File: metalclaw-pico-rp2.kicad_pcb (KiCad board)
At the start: 4 copper layers, 21 x 51 mm, 123 parts, among them J1 USB4105-GF-A, J2 FTSH-105-01-L-DV-K, SW1 PTS810SJM250SMTR LFS, SW2 PTS810SJM250SMTR LFS, U1 XC6220B331MR-G, U2 RP2354B, U3 APS6404L-3SQR-SN, Y1 ABM8-272-T3

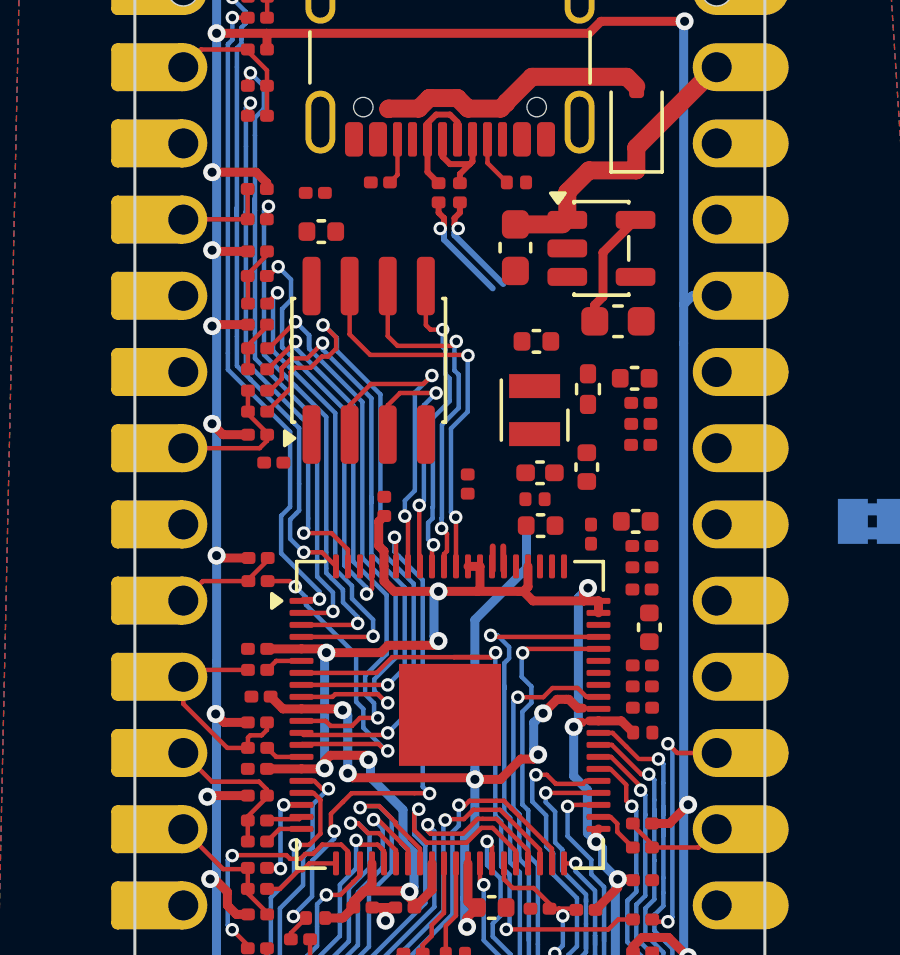
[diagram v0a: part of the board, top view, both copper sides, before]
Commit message: Route USB and last quadrant signals
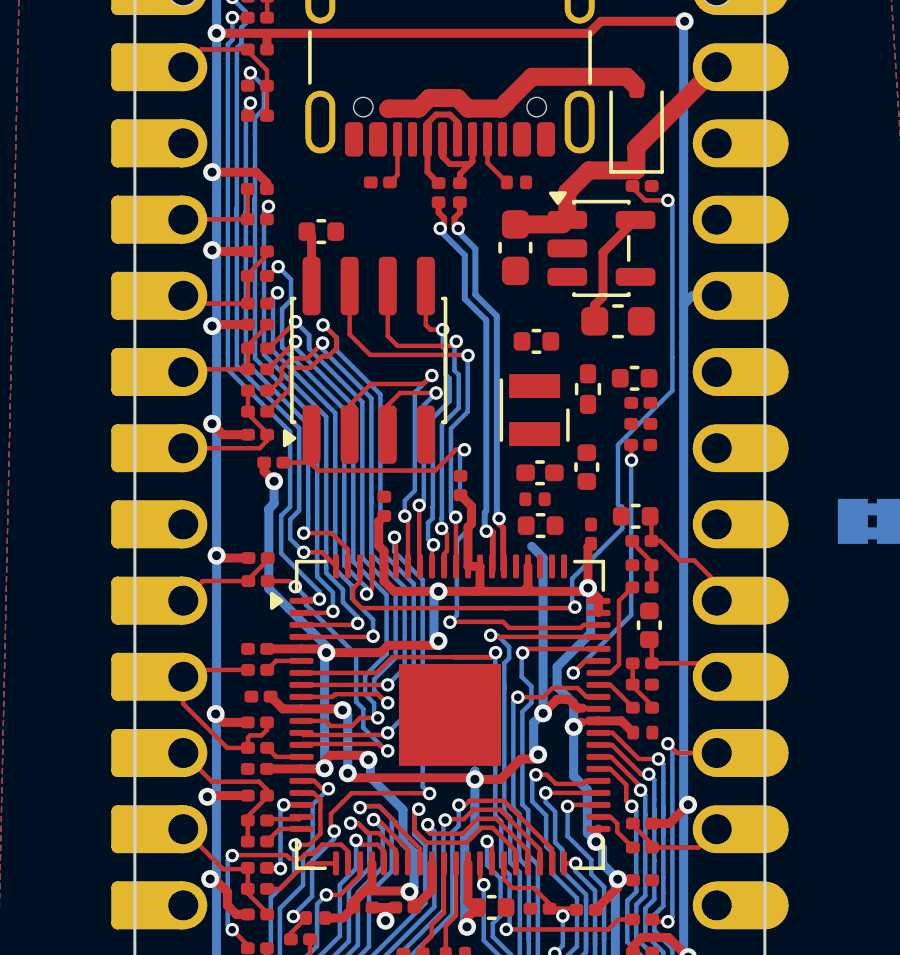
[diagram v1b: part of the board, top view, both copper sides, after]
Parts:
- moved R34 10.9 mm to (170.2, 81.2)
- moved C14 0.25 mm to (164.2, 91.2)
- moved C5 0.17 mm to (170.0, 92.2)
- moved R24 0.17 mm to (170.2, 93.1)
- moved C6 0.07 mm to (170.5, 95.9)
- moved C8 0.07 mm to (170.2, 93.9)
- moved R26 0.07 mm to (170.2, 97.2)
- moved R31 0.07 mm to (170.2, 94.6)
- moved C7 0.06 mm to (170.2, 97.9)
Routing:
- net Net-(U2-GPIO1): track 0.00 -> 25.5 mm, vias 0 -> 2
- net Net-(U2-GPIO47/ADC7): track 0.00 -> 18.8 mm, vias 0 -> 2
- net +3V3: track 72.3 -> 86.0 mm, vias 11 -> 12
- net /GP28: track 0.00 -> 9.42 mm, vias 0 -> 2
- net /USB_D+: track 4.55 -> 13.3 mm, vias 1 -> 2
- net /USB_D-: track 4.37 -> 13.0 mm, vias 1 -> 2
- net Net-(A1-GPIO27_ADC1): track 0.00 -> 4.18 mm
- net /GP27: track 0.00 -> 3.55 mm
- net Net-(A1-GPIO26_ADC0): track 0.00 -> 3.17 mm
- net Net-(U2-VREG_FB): track 31.9 -> 28.8 mm
- net /GP3: track 2.01 -> 4.27 mm
- net /GP4: track 1.75 -> 3.95 mm
- net Net-(C8-Pad2): track 0.00 -> 1.82 mm
- net Net-(C7-Pad2): track 0.00 -> 1.75 mm
- net /GP26: track 0.00 -> 1.47 mm

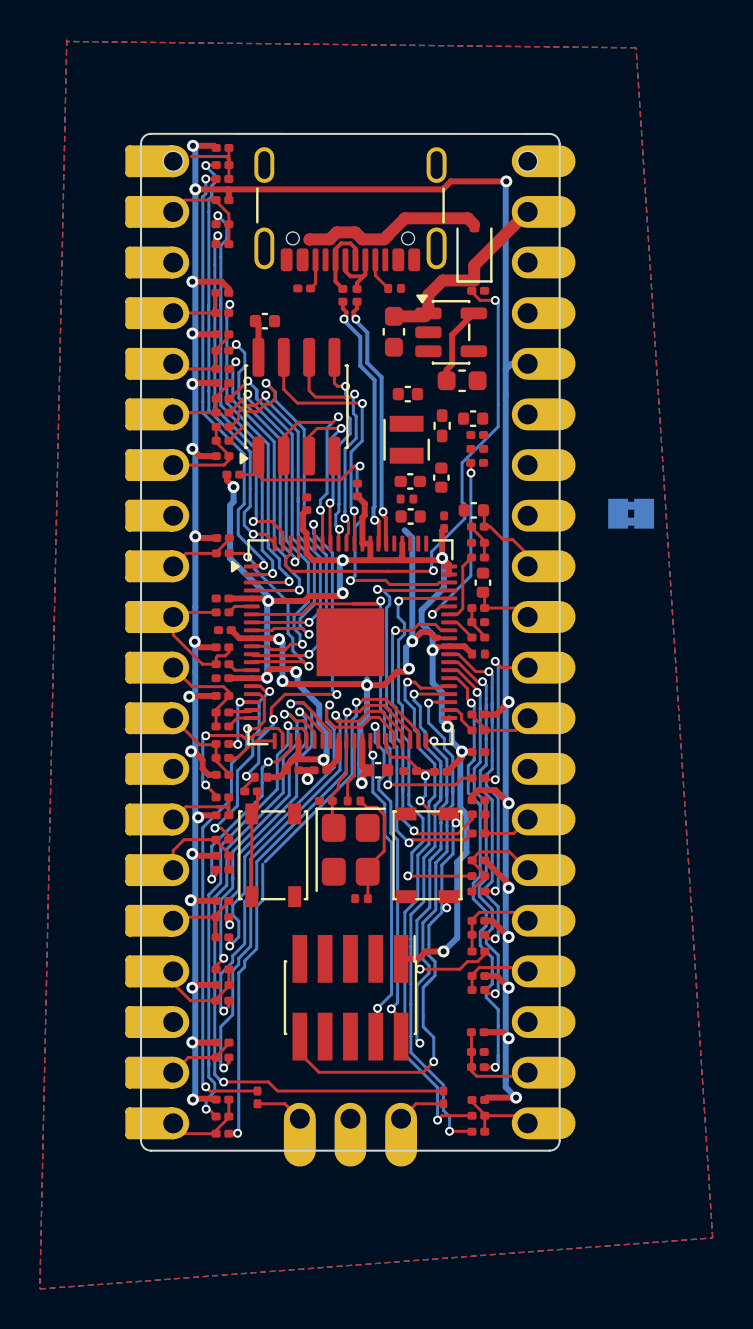
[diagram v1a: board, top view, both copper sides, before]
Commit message: Route all signals
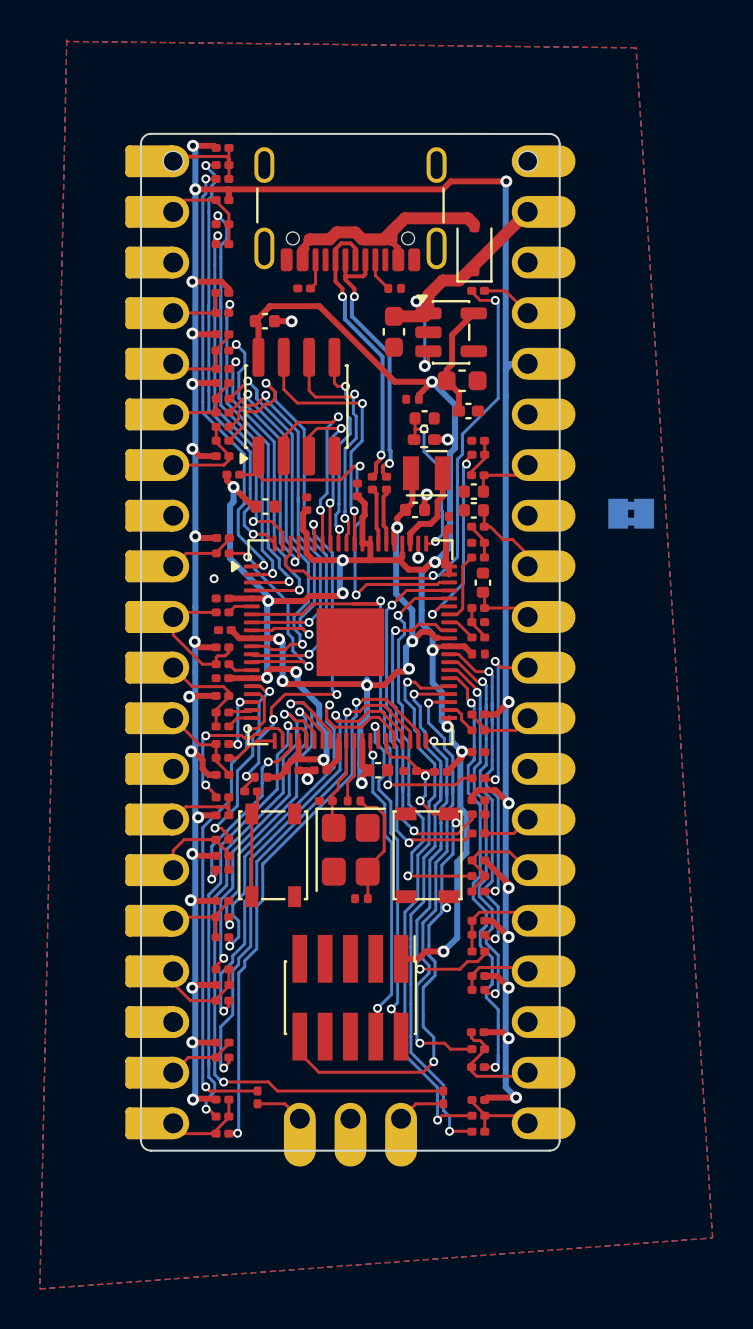
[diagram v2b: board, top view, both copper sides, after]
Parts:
- moved R80 9.54 mm to (165.6, 90.9)
- moved R81 9.54 mm to (164.9, 90.9)
- moved C12 9.10 mm to (159.6, 92.1)
- moved C15 5.01 mm to (166.9, 86.7), turned to 0 degrees
- moved C11 4.58 mm to (169.7, 87.3)
- moved C4 3.66 mm to (170.0, 91.3)
- moved C10 3.09 mm to (167.5, 87.6), turned to 180 degrees
- moved R23 2.02 mm to (170.2, 90.5)
- moved L1 1.96 mm to (167.6, 90.4), turned to 0 degrees
- moved R73 1.13 mm to (167.5, 88.7), turned to 180 degrees
- moved R32 0.41 mm to (170.2, 89.5)
- moved C9 0.41 mm to (170.2, 88.8)
- moved C13 0.40 mm to (167.1, 92.2)
- moved C22 0.23 mm to (168.7, 92.9)
- moved R67 0.14 mm to (170.2, 119.3), turned to 180 degrees
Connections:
- J1 pad A6: Net-(J1-D+-PadA6) -> /USB_D+
- J1 pad A7: Net-(J1-D--PadA7) -> /USB_D-
- J1 pad B6: Net-(J1-D+-PadA6) -> /USB_D+
- J1 pad B7: Net-(J1-D--PadA7) -> /USB_D-
- R80 pad 1: Net-(J1-D--PadA7) -> /USB_D-
- R80 pad 2: /USB_D- -> Net-(U2-USB_DM)
- R81 pad 1: Net-(J1-D+-PadA6) -> /USB_D+
- R81 pad 2: /USB_D+ -> Net-(U2-USB_DP)
- U2 pad 66: /USB_D- -> Net-(U2-USB_DM)
- U2 pad 67: /USB_D+ -> Net-(U2-USB_DP)
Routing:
- net +3V3: track 86.0 -> 112.5 mm, vias 12 -> 14
- net Net-(U2-VREG_AVDD): track 0.00 -> 8.21 mm, vias 0 -> 2
- net Net-(D1-A): track 9.15 -> 15.0 mm
- net Net-(U2-VREG_LX): track 0.00 -> 4.91 mm
- net VS: track 9.66 -> 14.3 mm, vias 0 -> 2
- net Net-(U2-VREG_FB): track 28.8 -> 33.1 mm, vias 6 -> 7
- net Net-(J1-D+-PadA6): track 3.95 -> 0.00 mm
- net Net-(A1-GPIO28_ADC2): track 0.00 -> 3.23 mm
- net Net-(J1-D--PadA7): track 3.22 -> 0.00 mm
- net Net-(U2-USB_DM): track 0.00 -> 2.85 mm
- net Net-(U2-USB_DP): track 0.00 -> 2.84 mm
- net /3V3_EN: track 0.00 -> 2.63 mm
- net Net-(U2-GPIO34): track 20.3 -> 22.8 mm
- net GND: track 1.53 -> 3.93 mm, vias 1 -> 5
- net Net-(C9-Pad2): track 0.00 -> 2.01 mm
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
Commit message: Rearrange power passives
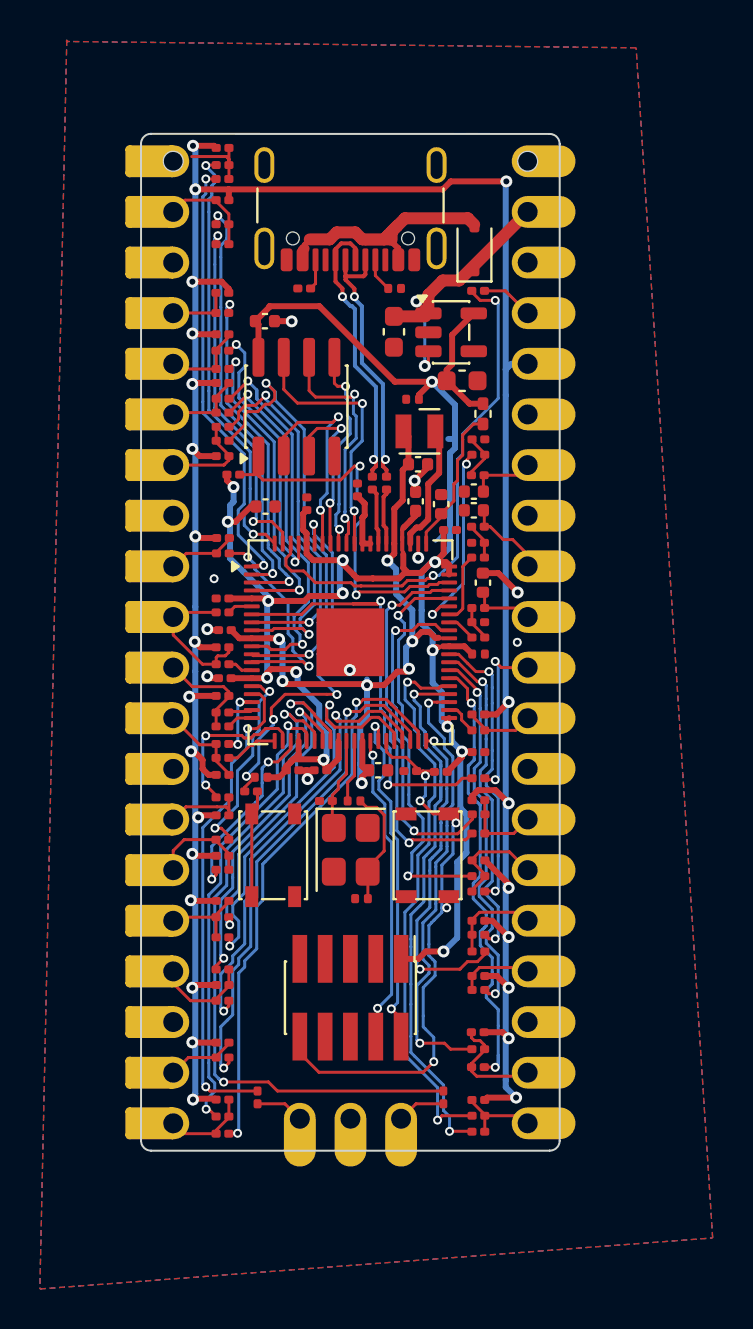
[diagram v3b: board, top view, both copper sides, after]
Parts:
- removed JP1: Jumper_2_Bridged, Jumper:SolderJumper-2_P1.3mm_Bridged2Bar_Pad1.0x1.5mm
- moved C11 5.25 mm to (167.1, 91.8), turned to -90 degrees
- moved C10 4.38 mm to (168.4, 91.9), turned to -90 degrees
- moved R73 3.22 mm to (170.5, 87.4), turned to -90 degrees
- moved C13 2.29 mm to (167.2, 89.9)
- moved L1 2.13 mm to (167.3, 88.3)
- moved C22 0.37 mm to (168.8, 93.2), turned to 180 degrees
- moved C18 0.12 mm to (157.5, 100.7)
- moved C9 0.07 mm to (170.2, 88.7), turned to 180 degrees
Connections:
- A1 pad 33: Net-(A1-AGND) -> GND
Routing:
- net GND: track 3.93 -> 8.82 mm, vias 5 -> 10
- net +3V3: track 112.5 -> 117.2 mm
- net Net-(U2-VREG_LX): track 4.91 -> 6.81 mm
- net Net-(U2-VREG_FB): track 33.1 -> 34.3 mm
- net Net-(U2-GPIO40/ADC0): track 15.1 -> 14.5 mm
- net Net-(U2-GPIO25): track 35.1 -> 34.5 mm
- net /BOOTSEL: track 19.0 -> 19.6 mm
- net Net-(U2-VREG_AVDD): track 8.21 -> 7.96 mm, vias 2 -> 0

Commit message: Fix overlap DRC errors
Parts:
- moved L1 0.09 mm to (167.3, 88.2)
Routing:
- net Net-(U2-GPIO46/ADC6): track 19.0 -> 20.2 mm
- net Net-(U2-GPIO41/ADC1): track 17.0 -> 17.5 mm
- net Net-(U2-VREG_AVDD): track 7.96 -> 7.46 mm
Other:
- board text removed: "${REFERENCE}"

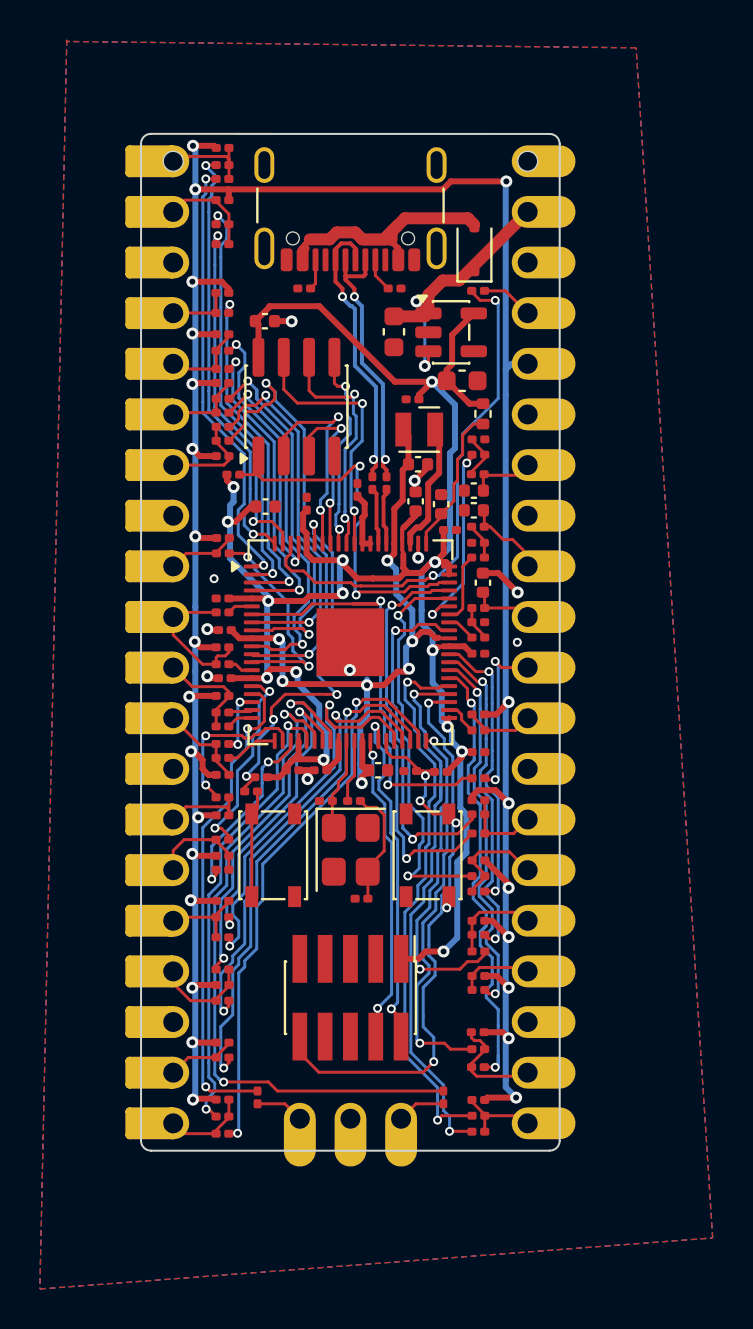
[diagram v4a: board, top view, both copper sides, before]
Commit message: Castellate A1 edge pads, fix D1 footprint (US2H), GND stitching, DRC clean
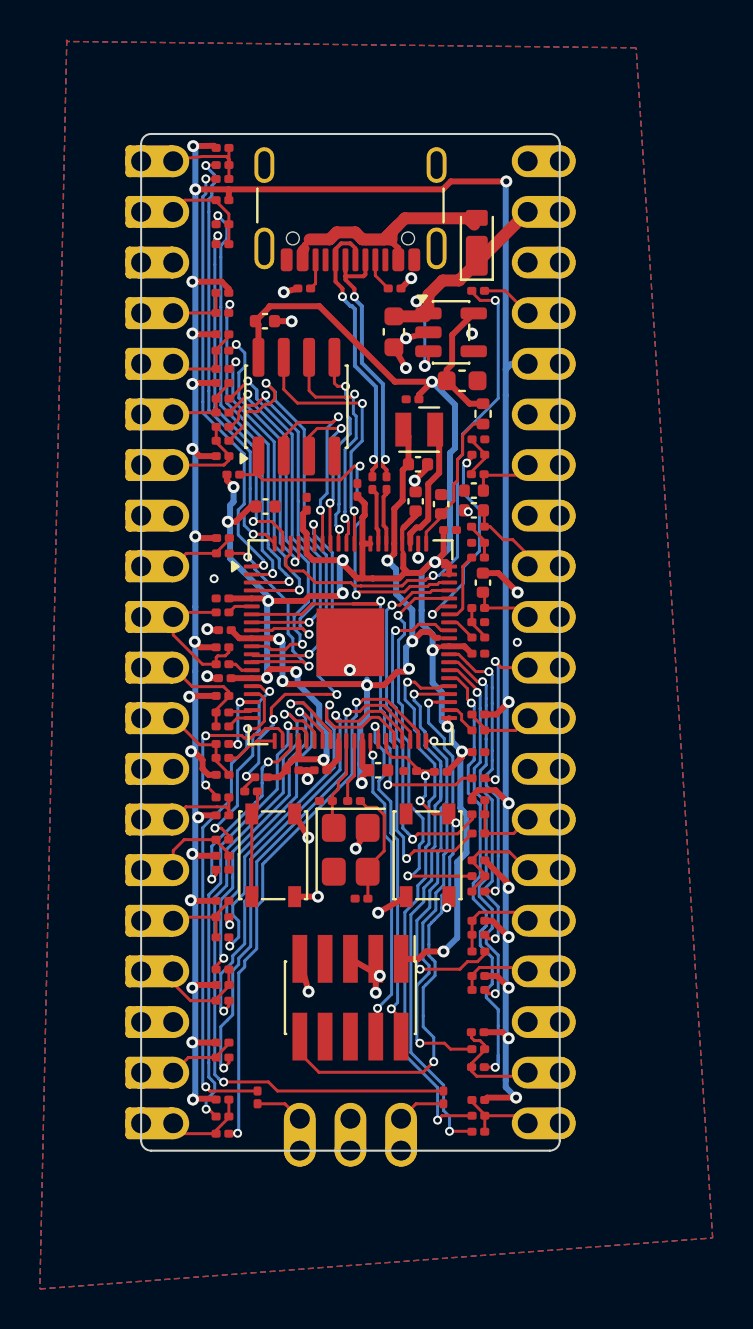
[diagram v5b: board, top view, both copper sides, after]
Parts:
- D1: footprint Diode_SMD:D_SOD-323F -> MetalClaw:D_US2H_CUHS20F30
- moved D1 0.35 mm to (170.2, 78.8)
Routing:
- net GND: track 8.82 -> 23.1 mm, vias 10 -> 23
- net +3V3: track 116.9 -> 118.6 mm
- net /GP0: track 3.86 -> 4.73 mm
- net /GP28: track 9.84 -> 10.5 mm
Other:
- outline, holes or cut-outs redrawn

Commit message: BOM: R83 CE pull-up 10k->2.2k, LCSC part numbers, L1 entry fix
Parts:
- R83: value 10k -> 2.2k

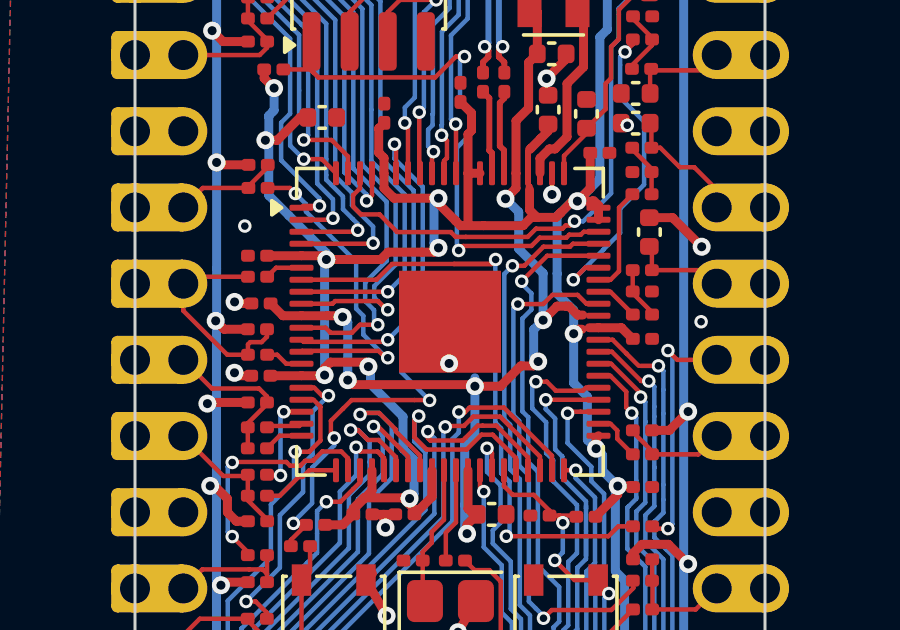
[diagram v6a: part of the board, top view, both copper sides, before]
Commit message: Add GND EP via grid; JLCPCB fab package (gerbers, BOM, CPL), fresh reports
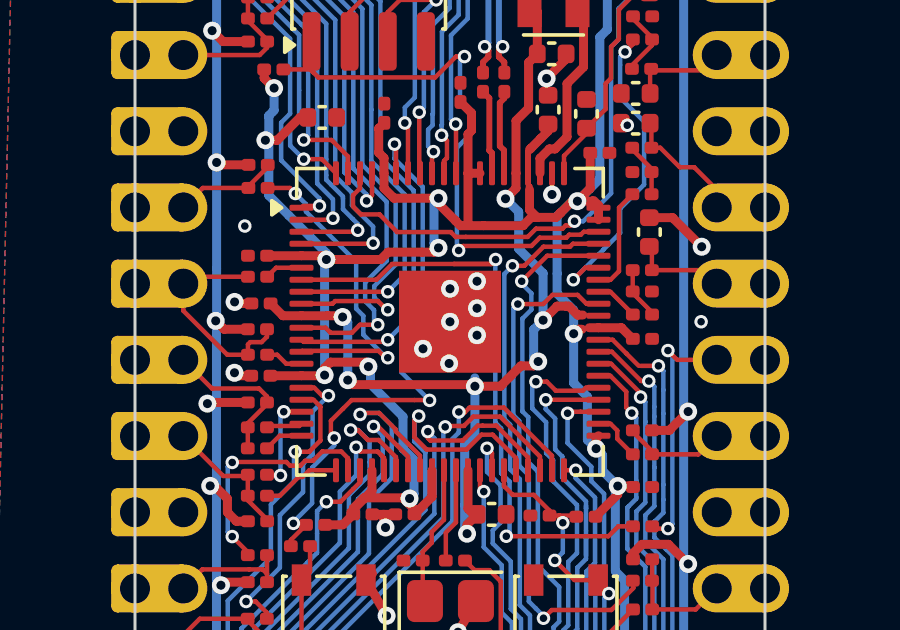
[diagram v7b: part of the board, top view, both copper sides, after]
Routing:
- net GND: vias 23 -> 29
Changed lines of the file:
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@@
+	)
+	(via
+		(at 164.71 98.42)
+		(size 0.6)
+		(drill 0.3)
+		(layers "F.Cu" "B.Cu")
+		(net 4)
 	)
 	(via
@@
 	)
 	(via
+		(at 164.71 99.32)
+		(size 0.6)
+		(drill 0.3)
+		(layers "F.Cu" "B.Cu")
+		(net 4)
+	)
+	(via
 		(at 161.709992 116.392073)
+		(size 0.6)
+		(drill 0.3)
+		(layers "F.Cu" "B.Cu")
+		(net 4)
+	)
+	(via
+		(at 162.91 99.77)
 		(size 0.6)
 		(drill 0.3)
@@
 	(via
 		(at 172.199 96.37)
+		(size 0.6)
+		(drill 0.3)
+		(layers "F.Cu" "B.Cu")
+		(net 4)
+	)
+	(via
+		(at 164.71 97.52)
 		(size 0.6)
 		(drill 0.3)
@@
 	)
 	(via
+		(at 163.81 97.77)
+		(size 0.6)
+		(drill 0.3)
+		(layers "F.Cu" "B.Cu")
+		(net 4)
+	)
+	(via
 		(at 162.177454 111.63)
 		(size 0.6)
@@
 		(size 0.6)
 		(drill 0.3)
+		(layers "F.Cu" "B.Cu")
+		(net 4)
+	)
+	(via
+		(at 163.81 98.87)
+		(size 0.6)
+		(drill 0.3)
